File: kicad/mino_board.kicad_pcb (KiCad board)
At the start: 2 copper layers, 224.8 x 91.4 mm, 35 parts, among them J1-2 Conn_01x04, J10 Conn_01x04, J2 Conn_01x05, J4 Conn_02x10_Counter_Clockwise, P1 LED, P2 LED, P3 LED, P4 LED, X1 SW_Push, Y1 SW_Push

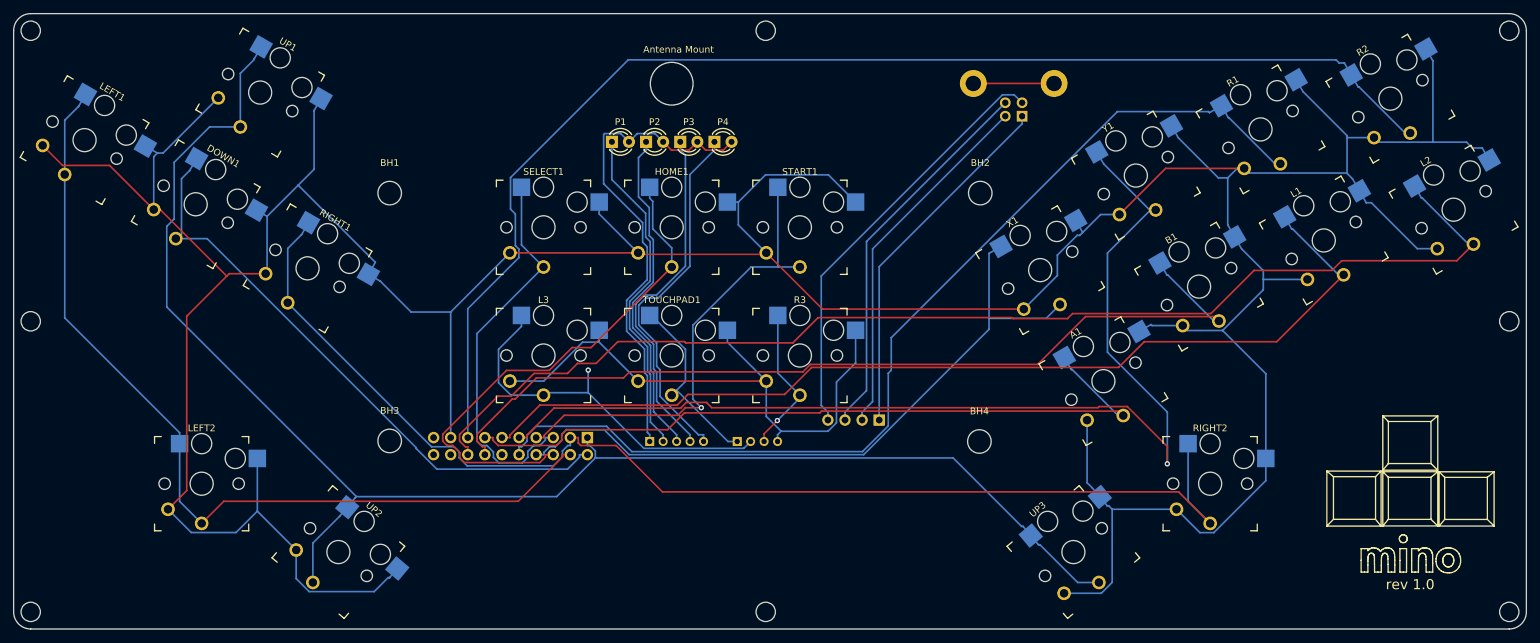
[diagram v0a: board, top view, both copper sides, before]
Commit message: Add footprints
Adding footprints pursuant to creating additional toggles and such
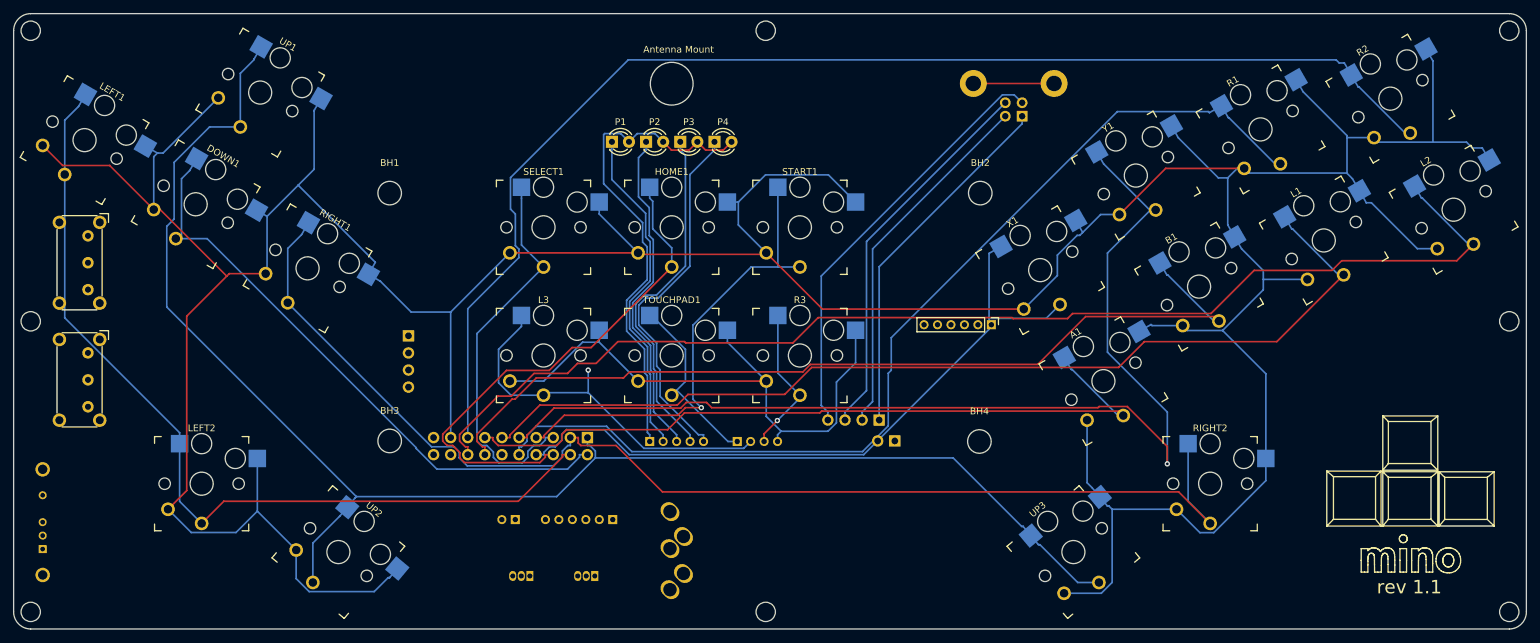
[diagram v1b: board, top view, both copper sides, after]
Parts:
- added AUDIO: Jack_3.5mm_CUI_SJ1-3535NG_Horizontal_CircularHoles, Connector_Audio:Jack_3.5mm_CUI_SJ1-3535NG_Horizontal_CircularHoles, B.Cu at (145.8, 150.4)
- added JAUDIO: PinHeader_1x06_P2.00mm_Vertical, Connector_PinHeader_2.00mm:PinHeader_1x06_P2.00mm_Vertical, F.Cu at (193.5, 111.0)
- added JPS51: PinHeader_1x06_P2.00mm_Vertical, Connector_PinHeader_2.00mm:PinHeader_1x06_P2.00mm_Vertical, B.Cu at (137.3, 140.0)
- added JPS52: PinHeader_1x02_P2.00mm_Vertical, Connector_PinHeader_2.00mm:PinHeader_1x02_P2.00mm_Vertical, B.Cu at (122.8, 140.0)
- added JSOCD: PinHeader_1x02_P2.54mm_Vertical, Connector_PinHeader_2.54mm:PinHeader_1x02_P2.54mm_Vertical, B.Cu at (179.2, 128.3)
- added JSTICKTYPE: PinHeader_1x04_P2.54mm_Vertical, Connector_PinHeader_2.54mm:PinHeader_1x04_P2.54mm_Vertical, B.Cu at (106.9, 112.6)
- added SW_SOCD: SW_E-Switch_EG1224_SPDT_Angled, Button_Switch_THT:SW_E-Switch_EG1224_SPDT_Angled, F.Cu at (59.3, 97.8)
- added SW_STICK: , EEC:E-Switch-EG1313-0, B.Cu at (50.1, 140.3)
- added SW_THUMBS: SW_E-Switch_EG1224_SPDT_Angled, Button_Switch_THT:SW_E-Switch_EG1224_SPDT_Angled, F.Cu at (59.3, 115.2)
- added TR_LFTHM: TO-92_Inline, Package_TO_SOT_THT:TO-92_Inline, B.Cu at (125.0, 148.3)
- added TR_RGTHM: TO-92_Inline, Package_TO_SOT_THT:TO-92_Inline, B.Cu at (134.6, 148.3)
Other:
- board text added: "rev 1.1"
- board text removed: "rev 1.0"

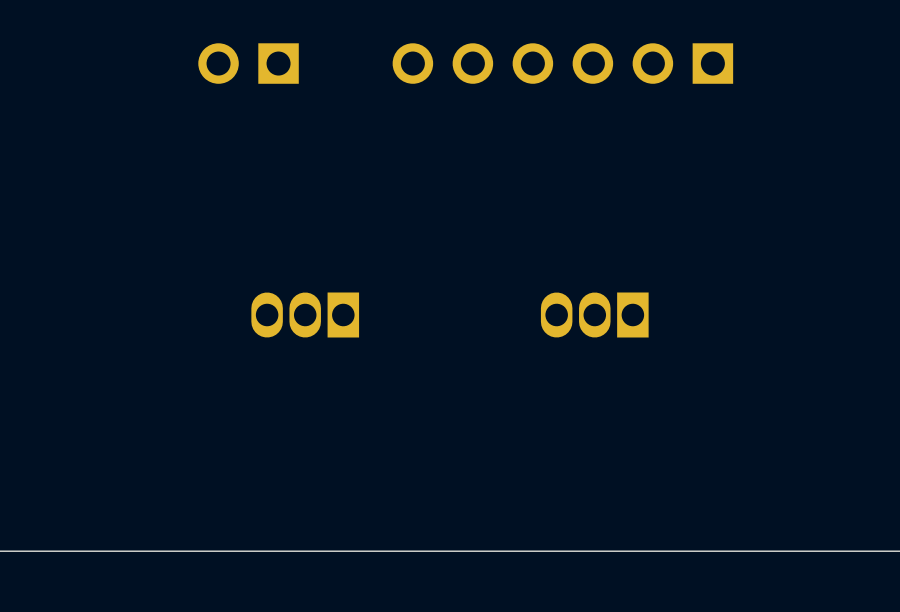
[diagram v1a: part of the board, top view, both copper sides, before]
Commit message: More Footprints
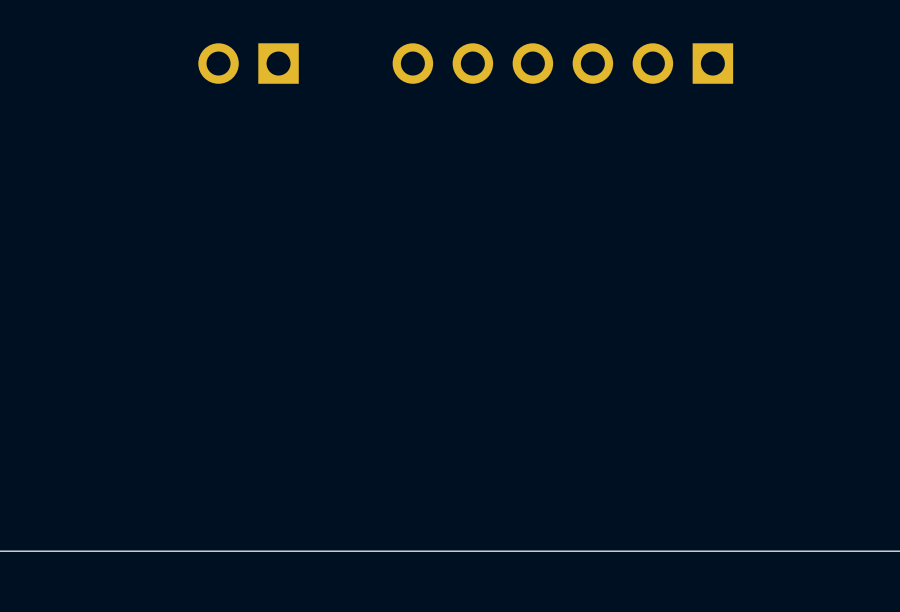
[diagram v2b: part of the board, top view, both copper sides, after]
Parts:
- removed TR_LFTHM, TR_RGTHM: TO-92_Inline, Package_TO_SOT_THT:TO-92_Inline

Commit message: More footprints again
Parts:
- added JEXTRAS: PinHeader_1x05_P2.00mm_Vertical, Connector_PinHeader_2.00mm:PinHeader_1x05_P2.00mm_Vertical, B.Cu at (106.9, 99.7)
- added JPS5JUMPER: PinHeader_1x02_P2.00mm_Vertical, Connector_PinHeader_2.00mm:PinHeader_1x02_P2.00mm_Vertical, B.Cu at (99.4, 110.9)
- added SW_THUMBR: SW_E-Switch_EG1224_SPDT_Angled, Button_Switch_THT:SW_E-Switch_EG1224_SPDT_Angled, F.Cu at (59.2, 133.0)
- moved SW_STICK 222.2 mm to (271.5, 122.7), turned to 270 degrees
- renumbered SW_THUMBS to SW_THUMBL

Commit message: Claw adjust
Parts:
- moved JPS5JUMPER 8.31 mm to (102.3, 118.7)
- moved SW_THUMBL 7.75 mm to (59.4, 122.9)
- moved SW_THUMBR 7.75 mm to (59.3, 140.8)
- moved SW_SOCD 7.75 mm to (59.4, 105.5)
- moved RIGHT1 3.27 mm to (90.7, 105.7)
- moved DOWN1 1.98 mm to (76.8, 91.8)
- moved UP1 1.98 mm to (86.4, 75.2)
- moved UP2 1.68 mm to (98.0, 145.6)
- moved LEFT2 1.68 mm to (77.7, 135.4)
- moved LEFT1 1.21 mm to (58.7, 84.8)
- moved RIGHT2 0.64 mm to (226.1, 135.3)
- moved UP3 0.64 mm to (205.8, 145.4)
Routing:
- net Net-(A1-Pad2): track 653.5 -> 0.00 mm
- net Net-(J4-Pad1): track 226.4 -> 0.00 mm
- net Net-(J4-Pad15): track 188.3 -> 0.00 mm
- net Net-(J4-Pad3): track 182.6 -> 0.00 mm
- net Net-(J4-Pad16): track 179.0 -> 0.00 mm
- net Net-(J4-Pad9): track 160.8 -> 0.00 mm, vias 1 -> 0
- net Net-(J4-Pad10): track 150.2 -> 0.00 mm
- net Net-(J4-Pad11): track 147.9 -> 0.00 mm
- net Net-(B1-Pad1): track 134.1 -> 0.00 mm
- net Net-(J4-Pad4): track 132.5 -> 0.00 mm
- net Net-(A1-Pad1): track 111.1 -> 0.00 mm
- net Net-(J4-Pad8): track 103.6 -> 0.00 mm
- net Net-(DOWN1-Pad1): track 89.2 -> 0.00 mm
- net Net-(J10-Pad4): track 88.4 -> 0.00 mm
- net Net-(HOME1-Pad1): track 77.5 -> 0.00 mm
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
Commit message: WIring and changes
Wire everything except audio, remove the PS5 board bits temporarily until I become more familiar with how it works.
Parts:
- removed JEXTRAS: PinHeader_1x05_P2.00mm_Vertical, Connector_PinHeader_2.00mm:PinHeader_1x05_P2.00mm_Vertical
- removed JPS51: PinHeader_1x06_P2.00mm_Vertical, Connector_PinHeader_2.00mm:PinHeader_1x06_P2.00mm_Vertical
- removed JPS52, JPS5JUMPER: PinHeader_1x02_P2.00mm_Vertical, Connector_PinHeader_2.00mm:PinHeader_1x02_P2.00mm_Vertical

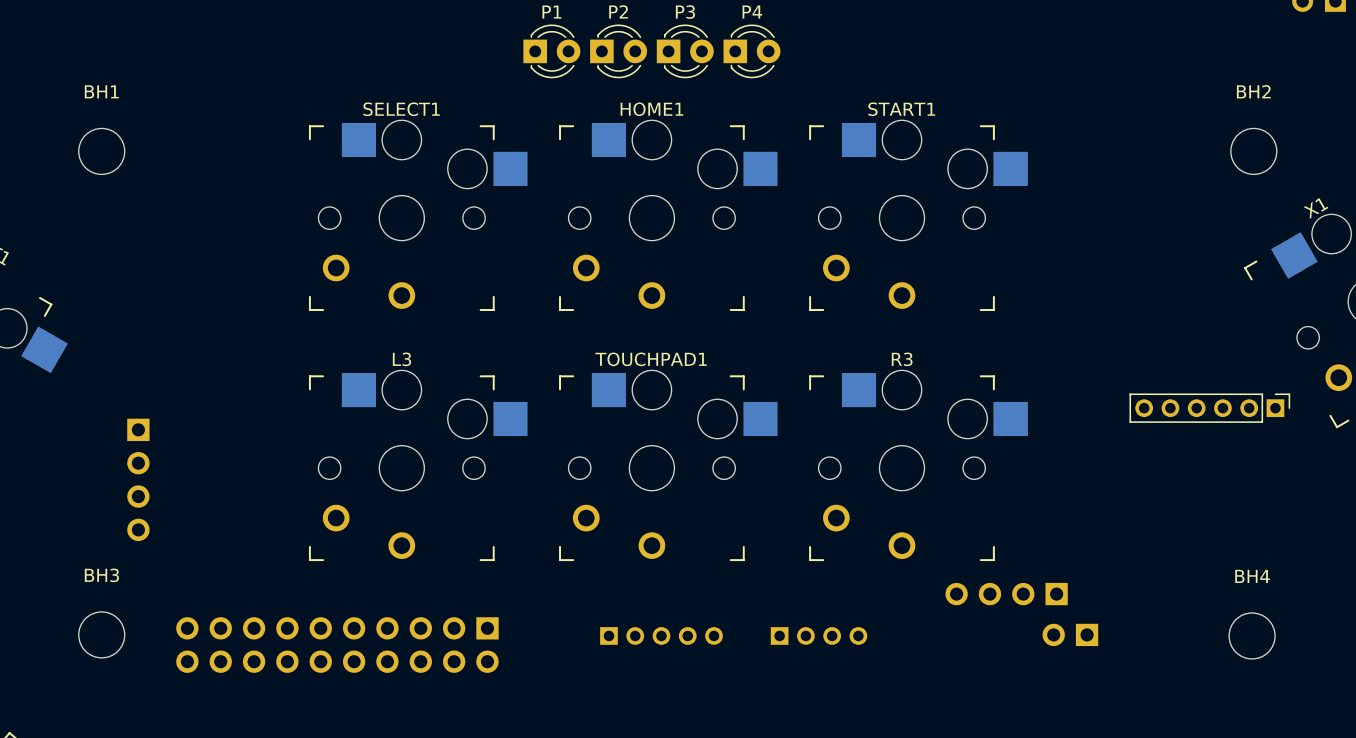
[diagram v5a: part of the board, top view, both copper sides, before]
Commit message: Remove mounting holes
The fit of the spacers to the base board turned out better than expected, so these are not needed.
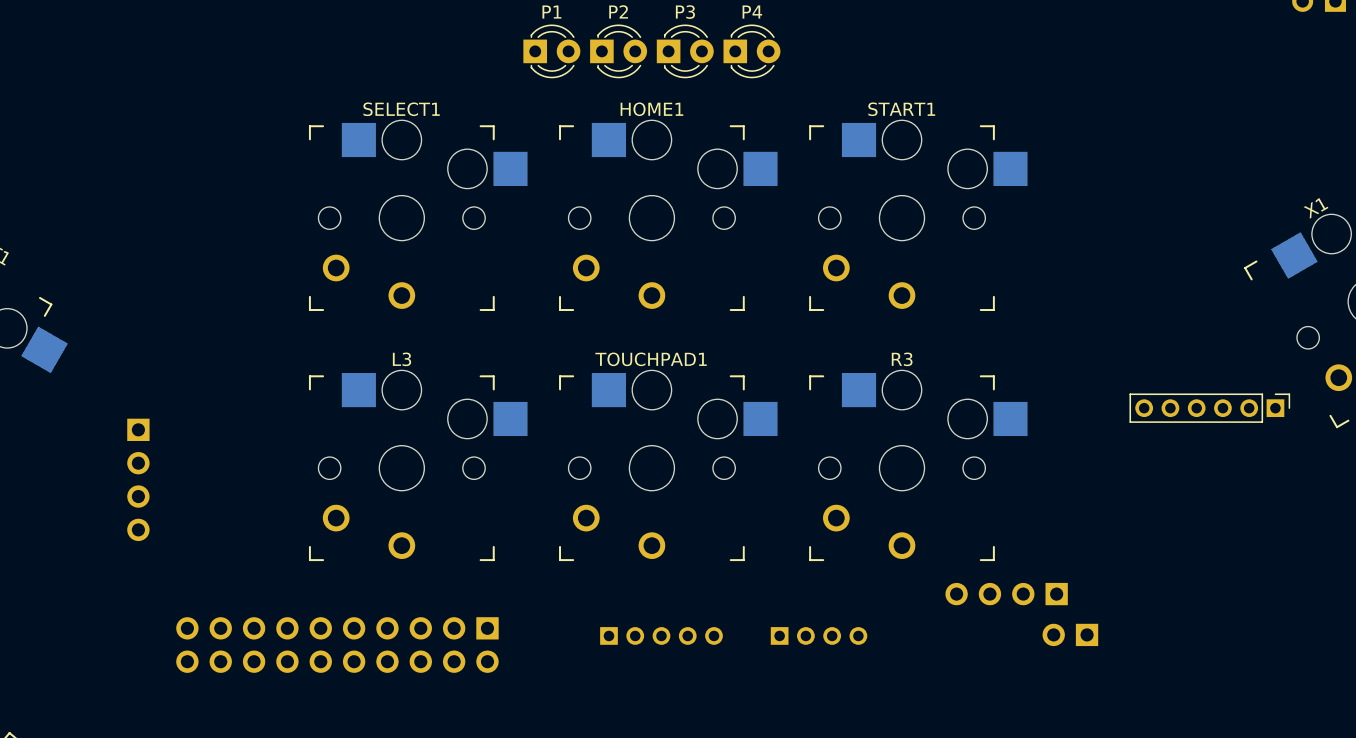
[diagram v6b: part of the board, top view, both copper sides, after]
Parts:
- removed BH1, BH2, BH3, BH4: MountingHole_3.5mm, MountingHole:MountingHole_3.5mm

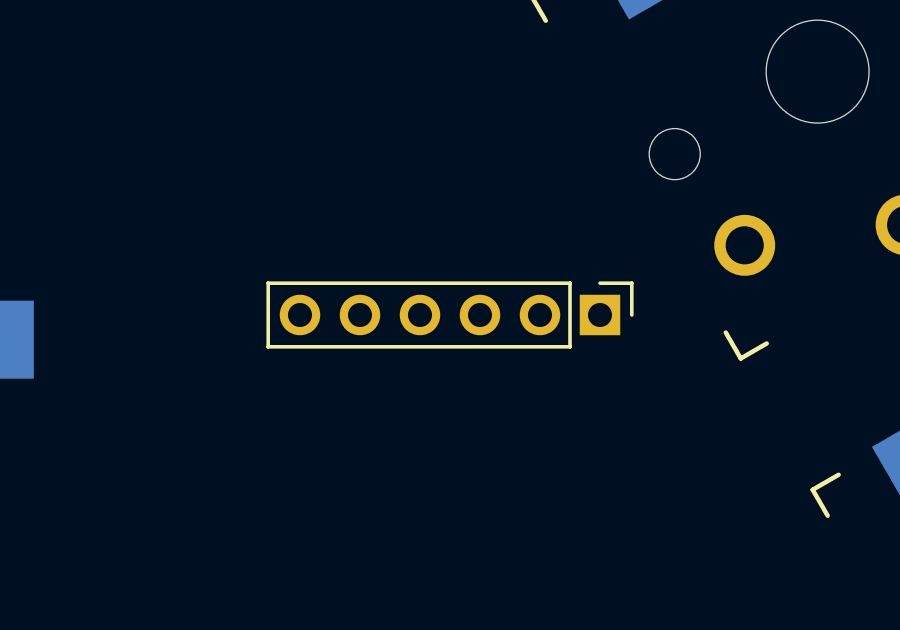
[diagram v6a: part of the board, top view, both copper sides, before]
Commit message: Flips
Missed a flipped connector
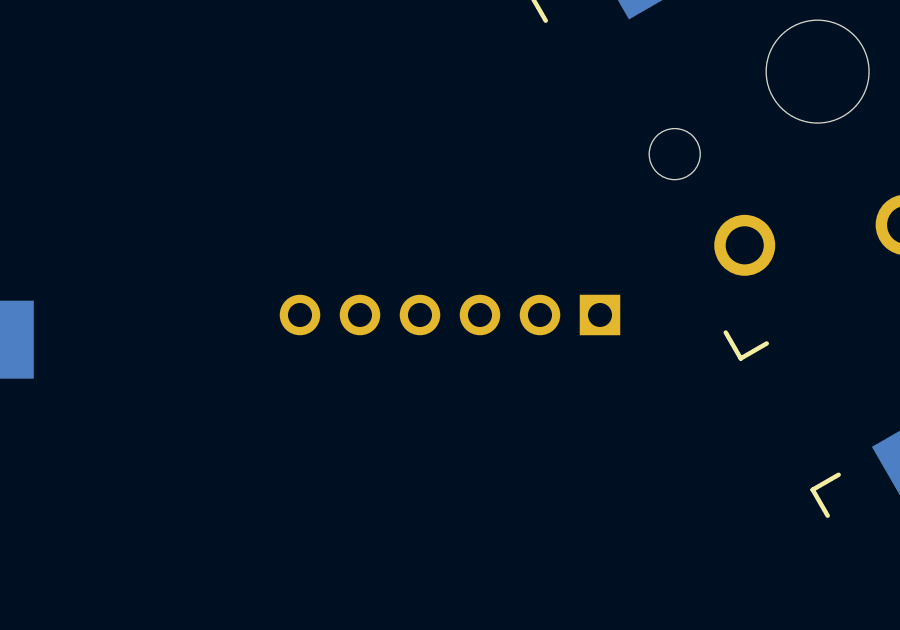
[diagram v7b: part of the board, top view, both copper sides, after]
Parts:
- JAUDIO: moved to B.Cu
- turned JAUDIO to 90 degrees
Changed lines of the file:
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@@
     )
   )
-  (module Connector_PinHeader_2.00mm:PinHeader_1x06_P2.00mm_Vertical (layer F.Cu)
-    (at 193.548 110.998 270)
+  (module Connector_PinHeader_2.00mm:PinHeader_1x06_P2.00mm_Vertical (layer B.Cu)
+    (at 193.548 110.998 90)
     (descr "Through hole straight pin header, 1x06, 2.00mm pitch, single row")
     (tags "Through hole pin header THT 1x06 2.00mm single row")
-    (fp_text reference JAUDIO (at 0 -2.06 90) (layer B.SilkS)
+    (fp_text reference JAUDIO (at 0 2.06 -90) (layer B.SilkS)
       (effects (font (size 1 1) (thickness 0.15)) (justify mirror))
     )
-    (fp_text value PinHeader_1x06_P2.00mm_Vertical (at 0 12.06 90) (layer F.Fab)
-      (effects (font (size 1 1) (thickness 0.15)))
+    (fp_text value PinHeader_1x06_P2.00mm_Vertical (at 0 -12.06 270) (layer B.Fab)
+      (effects (font (size 1 1) (thickness 0.15)) (justify mirror))
     )
-    (fp_line (start -0.5 -1) (end 1 -1) (layer F.Fab) (width 0.1))
-    (fp_line (start 1 -1) (end 1 11) (layer F.Fab) (width 0.1))
-    (fp_line (start 1 11) (end -1 11) (layer F.Fab) (width 0.1))
-    (fp_line (start -1 11) (end -1 -0.5) (layer F.Fab) (width 0.1))
-    (fp_line (start -1 -0.5) (end -0.5 -1) (layer F.Fab) (width 0.1))
-    (fp_line (start -1.06 11.06) (end 1.06 11.06) (layer F.SilkS) (width 0.12))
-    (fp_line (start -1.06 1) (end -1.06 11.06) (layer F.SilkS) (width 0.12))
-    (fp_line (start 1.06 1) (end 1.06 11.06) (layer F.SilkS) (width 0.12))
-    (fp_line (start -1.06 1) (end 1.06 1) (layer F.SilkS) (width 0.12))
-    (fp_line (start -1.06 0) (end -1.06 -1.06) (layer F.SilkS) (width 0.12))
-    (fp_line (start -1.06 -1.06) (end 0 -1.06) (layer F.SilkS) (width 0.12))
-    (fp_line (start -1.5 -1.5) (end -1.5 11.5) (layer F.CrtYd) (width 0.05))
-    (fp_line (start -1.5 11.5) (end 1.5 11.5) (layer F.CrtYd) (width 0.05))
-    (fp_line (start 1.5 11.5) (end 1.5 -1.5) (layer F.CrtYd) (width 0.05))
-    (fp_line (start 1.5 -1.5) (end -1.5 -1.5) (layer F.CrtYd) (width 0.05))
-    (fp_text user %R (at 0 5) (layer F.Fab)
-      (effects (font (size 1 1) (thickness 0.15)))
+    (fp_line (start -0.5 1) (end 1 1) (layer B.Fab) (width 0.1))
+    (fp_line (start 1 1) (end 1 -11) (layer B.Fab) (width 0.1))
+    (fp_line (start 1 -11) (end -1 -11) (layer B.Fab) (width 0.1))
+    (fp_line (start -1 -11) (end -1 0.5) (layer B.Fab) (width 0.1))
+    (fp_line (start -1 0.5) (end -0.5 1) (layer B.Fab) (width 0.1))
+    (fp_line (start -1.06 -11.06) (end 1.06 -11.06) (layer B.SilkS) (width 0.12))
+    (fp_line (start -1.06 -1) (end -1.06 -11.06) (layer B.SilkS) (width 0.12))
+    (fp_line (start 1.06 -1) (end 1.06 -11.06) (layer B.SilkS) (width 0.12))
+    (fp_line (start -1.06 -1) (end 1.06 -1) (layer B.SilkS) (width 0.12))
+    (fp_line (start -1.06 0) (end -1.06 1.06) (layer B.SilkS) (width 0.12))
+    (fp_line (start -1.06 1.06) (end 0 1.06) (layer B.SilkS) (width 0.12))
+    (fp_line (start -1.5 1.5) (end -1.5 -11.5) (layer B.CrtYd) (width 0.05))
+    (fp_line (start -1.5 -11.5) (end 1.5 -11.5) (layer B.CrtYd) (width 0.05))
+    (fp_line (start 1.5 -11.5) (end 1.5 1.5) (layer B.CrtYd) (width 0.05))
+    (fp_line (start 1.5 1.5) (end -1.5 1.5) (layer B.CrtYd) (width 0.05))
+    (fp_text user %R (at 0 -5) (layer B.Fab)
+      (effects (font (size 1 1) (thickness 0.15)) (justify mirror))
     )
-    (pad 6 thru_hole oval (at 0 10 270) (size 1.35 1.35) (drill 0.8) (layers *.Cu *.Mask))
-    (pad 5 thru_hole oval (at 0 8 270) (size 1.35 1.35) (drill 0.8) (layers *.Cu *.Mask))
-    (pad 4 thru_hole oval (at 0 6 270) (size 1.35 1.35) (drill 0.8) (layers *.Cu *.Mask))
-    (pad 3 thru_hole oval (at 0 4 270) (size 1.35 1.35) (drill 0.8) (layers *.Cu *.Mask))
-    (pad 2 thru_hole oval (at 0 2 270) (size 1.35 1.35) (drill 0.8) (layers *.Cu *.Mask))
-    (pad 1 thru_hole rect (at 0 0 270) (size 1.35 1.35) (drill 0.8) (layers *.Cu *.Mask))
+    (pad 6 thru_hole oval (at 0 -10 90) (size 1.35 1.35) (drill 0.8) (layers *.Cu *.Mask))
+    (pad 5 thru_hole oval (at 0 -8 90) (size 1.35 1.35) (drill 0.8) (layers *.Cu *.Mask))
+    (pad 4 thru_hole oval (at 0 -6 90) (size 1.35 1.35) (drill 0.8) (layers *.Cu *.Mask))
+    (pad 3 thru_hole oval (at 0 -4 90) (size 1.35 1.35) (drill 0.8) (layers *.Cu *.Mask))
+    (pad 2 thru_hole oval (at 0 -2 90) (size 1.35 1.35) (drill 0.8) (layers *.Cu *.Mask))
+    (pad 1 thru_hole rect (at 0 0 90) (size 1.35 1.35) (drill 0.8) (layers *.Cu *.Mask))
     (model ${KISYS3DMOD}/Connector_PinHeader_2.00mm.3dshapes/PinHeader_1x06_P2.00mm_Vertical.wrl
       (at (xyz 0 0 0))

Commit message: Moving stuff around
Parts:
- SW_SOCD, SW_THUMBL, SW_THUMBR: moved to B.Cu
- moved SW_SOCD 114.6 mm to (170.3, 76.6), turned to 0 degrees
- moved SW_THUMBL 80.2 mm to (124.9, 76.6), turned to 0 degrees
- moved SW_THUMBR 80.0 mm to (107.1, 76.6), turned to 0 degrees
- moved SW_STICK 75.9 mm to (219.3, 67.6), turned to 0 degrees
